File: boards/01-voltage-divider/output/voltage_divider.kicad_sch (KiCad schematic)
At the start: 4 parts, among them J1 IN, J2 OUT

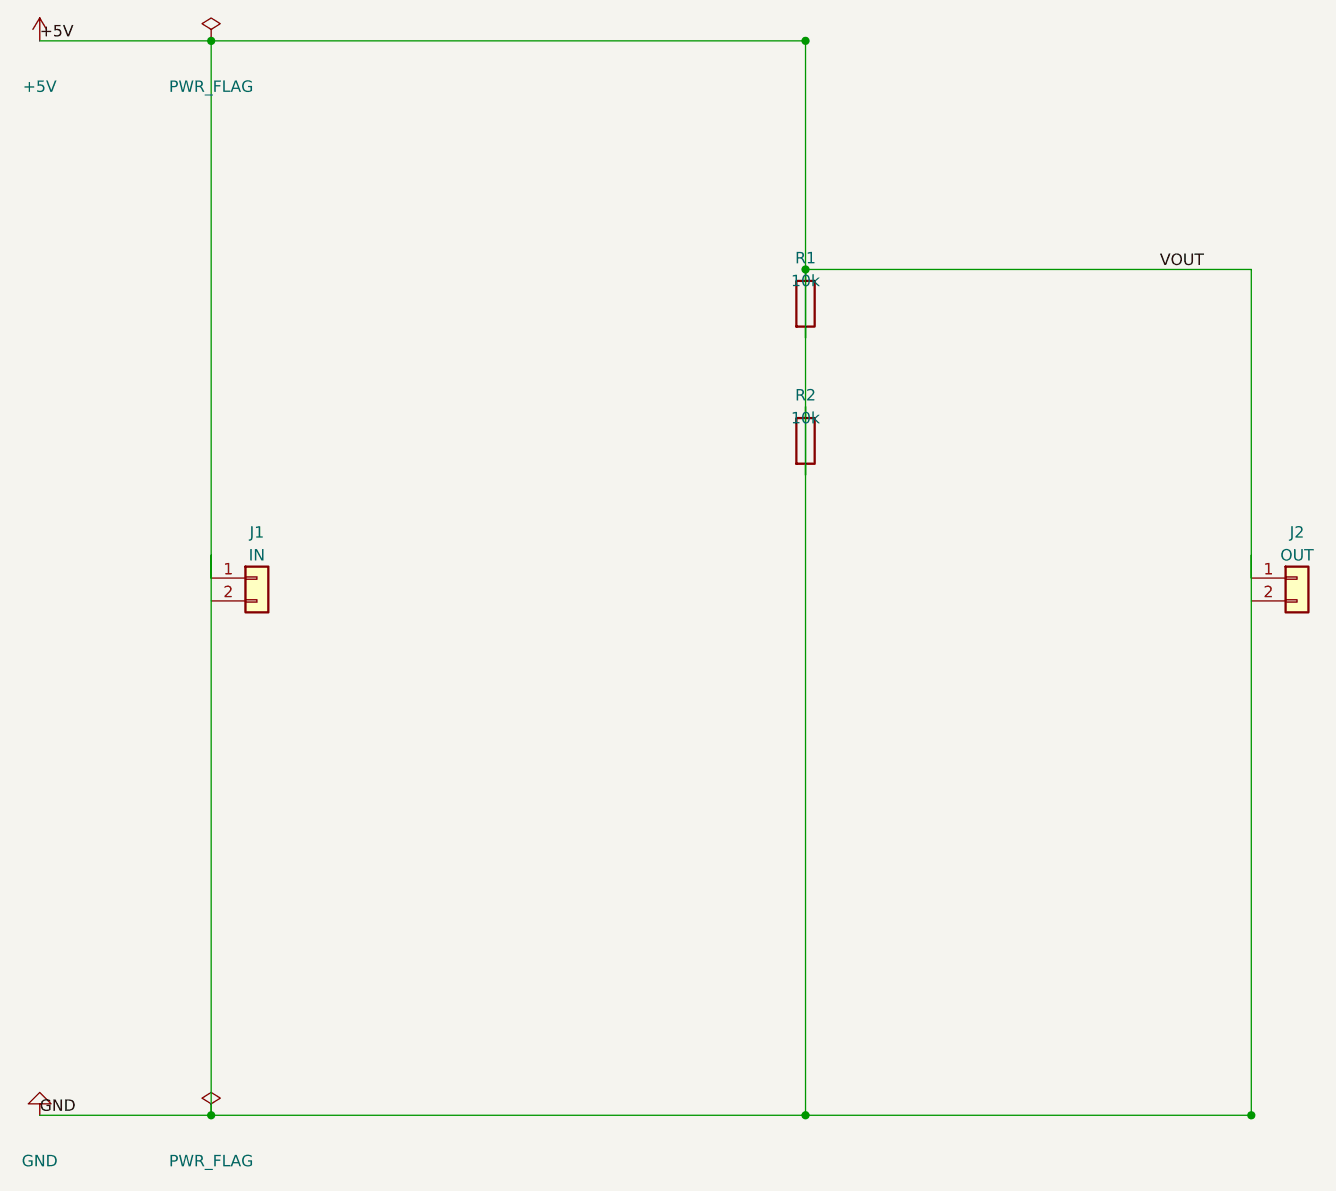
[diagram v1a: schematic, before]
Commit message: fix(board-01): migrate to negotiated router + pour-net carve-out (restore gold standard) (#3034)
* fix(board-01): migrate route step to negotiated router

Board 01's generate_design.py was calling the deprecated route_all()
entry point, which silently produced zero routed segments — VOUT in
particular had no traces on the on-disk PCB despite the script's
success counter reading 2/3 from pre-placed power-rail data.

Three coupled changes restore the gold-standard end-state:

1. Call route_all_negotiated(per_net_timeout=30.0, timeout=240.0) so
   per-net deadlines are enforced (Issue #2794 / #2775).
2. Apply the same pour-net carve-out the kct route CLI uses
   (Issue #1841): VIN and VOUT are classified as POWER by the name
   regex but this board has no copper zones, so they must route as
   signals via router._pour_nets_without_zones.
3. After routing, call cleanup_artifacts() (drops net-0 escape
   pre-pass orphans) and pass nets_to_route_ids to get_statistics()
   so the success metric matches kct route's reporting and excludes
   the intentionally-skipped GND from the denominator.

A VOUT-segment guard is added after the file write so any future
regression to the silent-zero-segments mode is loud, not silent.

Verified:
- python boards/01-voltage-divider/generate_design.py exits 0 and
  prints "Routing: SUCCESS" (was "PARTIAL: Routed 0/2 nets").
- Routed PCB has 29 (segment ...) entries (was 0); VOUT has 8.
- kct check --mfr jlcpcb: 0 errors, 4 pad_grid warnings (unchanged).
- kct fleet status: 2/3 nets complete (VIN, VOUT). GND remains
  intentionally skipped — the pre-regression gold standard never
  routed GND either (golden commit 55ac7a92: 3 VIN segs + 6 VOUT
  segs, 0 GND).

* feat(board-01): add manufacturing bundle (mfr=jlcpcb)

Generated via:
  kct export boards/01-voltage-divider/output/voltage_divider_routed.kicad_pcb --mfr jlcpcb

Brings board 01 to ship-ready parity with the other audit-tracked boards
(04/06/07) that already have manufacturing/ commi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
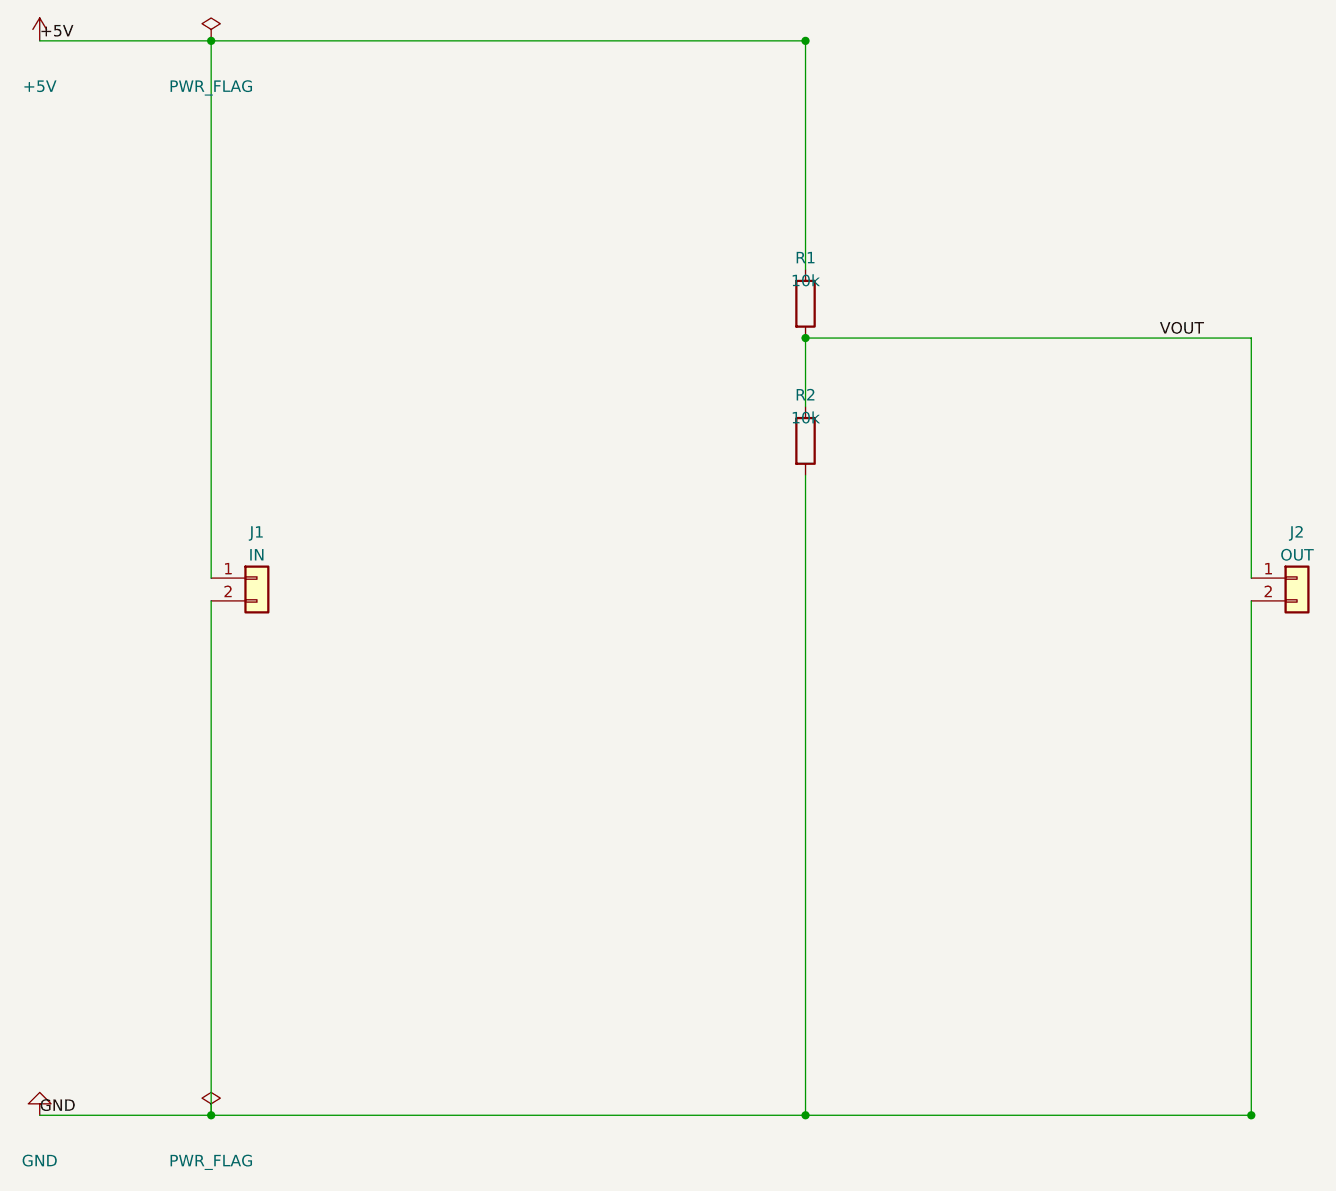
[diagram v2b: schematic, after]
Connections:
- net +5V: no longer J2.1 (Pin_1), R1.2, R2.1, R2.2
- net GND: now reaches J1.2 (Pin_2)
- net GND: now also J2.2 (Pin_2), R2.2
- new net VOUT: J2.1 (Pin_1), R1.2, R2.1
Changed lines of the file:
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@@
 		(instances
 			(project "project"
-				(path "/149338e6-b8c0-4787-8002-a53f5b29e82c" (reference "J1") (unit 1)
+				(path "/eab735e0-f8d9-4950-9b5d-95808fbf7dfa" (reference "J1") (unit 1)
 				)
 			)
@@
 		(instances
 			(project "project"
-				(path "/149338e6-b8c0-4787-8002-a53f5b29e82c" (reference "R1") (unit 1)
+				(path "/eab735e0-f8d9-4950-9b5d-95808fbf7dfa" (reference "R1") (unit 1)
 				)
 			)
@@
 		(instances
 			(project "project"
-				(path "/149338e6-b8c0-4787-8002-a53f5b29e82c" (reference "R2") (unit 1)
+				(path "/eab735e0-f8d9-4950-9b5d-95808fbf7dfa" (reference "R2") (unit 1)
 				)
 			)
@@
 		(instances
 			(project "project"
-				(path "/149338e6-b8c0-4787-8002-a53f5b29e82c" (reference "J2") (unit 1)
+				(path "/eab735e0-f8d9-4950-9b5d-95808fbf7dfa" (reference "J2") (unit 1)
 				)
 			)
@@
 		(instances
 			(project "project"
-				(path "/149338e6-b8c0-4787-8002-a53f5b29e82c" (reference "#PWR01") (unit 1)
+				(path "/eab735e0-f8d9-4950-9b5d-95808fbf7dfa" (reference "#PWR01") (unit 1)
 				)
 			)
@@
 		(instances
 			(project "project"
-				(path "/149338e6-b8c0-4787-8002-a53f5b29e82c" (reference "#PWR02") (unit 1)
+				(path "/eab735e0-f8d9-4950-9b5d-95808fbf7dfa" (reference "#PWR02") (unit 1)
 				)
 			)
@@
 		(instances
 			(project "project"
-				(path "/149338e6-b8c0-4787-8002-a53f5b29e82c" (reference "#PWR03") (unit 1)
+				(path "/eab735e0-f8d9-4950-9b5d-95808fbf7dfa" (reference "#PWR03") (unit 1)
 				)
 			)
@@
 		(instances
 			(project "project"
-				(path "/149338e6-b8c0-4787-8002-a53f5b29e82c" (reference "#PWR04") (unit 1)
+				(path "/eab735e0-f8d9-4950-9b5d-95808fbf7dfa" (reference "#PWR04") (unit 1)
 				)
 			)
@@
 	)
 	(wire
-		(pts (xy 44.45 87.63) (xy 44.45 149.86))
-		(stroke
-			(width 0)
-			(type default)
-		)
-	)
-	(wire
-		(pts (xy 110.49 63.5) (xy 110.49 30.48))
-		(stroke
-			(width 0)
-			(type default)
-		)
-	)
-	(wire
-		(pts (xy 110.49 55.88) (xy 110.49 78.74))
-		(stroke
-			(width 0)
-			(type default)
-		)
-	)
-	(wire
-		(pts (xy 110.49 71.12) (xy 110.49 149.86))
-		(stroke
-			(width 0)
-			(type default)
-		)
-	)
-	(wire
-		(pts (xy 110.49 55.88) (xy 160.02 55.88))
-		(stroke
-			(width 0)
-			(type default)
-		)
-	)
-	(wire
-		(pts (xy 160.02 55.88) (xy 160.02 90.17))
-		(stroke
-			(width 0)
-			(type default)
-		)
-	)
-	(wire
-		(pts (xy 160.02 87.63) (xy 160.02 149.86))
+		(pts (xy 44.45 92.71) (xy 44.45 149.86))
+		(stroke
+			(width 0)
+			(type default)
+		)
+	)
+	(wire
+		(pts (xy 110.49 55.88) (xy 110.49 30.48))
+		(stroke
+			(width 0)
+			(type default)
+		)
+	)
+	(wire
+		(pts (xy 110.49 63.5) (xy 110.49 71.12))
+		(stroke
+			(width 0)
+			(type default)
+		)
+	)
+	(wire
+		(pts (xy 110.49 78.74) (xy 110.49 149.86))
+		(stroke
+			(width 0)
+			(type default)
+		)
+	)
+	(wire
+		(pts (xy 110.49 63.5) (xy 160.02 63.5))
+		(stroke
+			(width 0)
+			(type default)
+		)
+	)
+	(wire
+		(pts (xy 160.02 63.5) (xy 160.02 90.17))
+		(stroke
+			(width 0)
+			(type default)
+		)
+	)
+	(wire
+		(pts (xy 160.02 92.71) (xy 160.02 149.86))
 		(stroke
 			(width 0)
@@
 	)
 	(junction
-		(at 110.49 55.88)
+		(at 110.49 63.5)
 		(diameter 0)
 	)
@@
 	)
 	(label "VOUT"
-		(at 149.86 55.88 0)
+		(at 149.86 63.5 0)
 		(fields_autoplaced yes)
 		(effects
@@
 	)
 	(sheet_instances
-		(path "/149338e6-b8c0-4787-8002-a53f5b29e82c" (page 1)
-		)
-	)
+		(path "/eab735e0-f8d9-4950-9b5d-95808fbf7dfa" (page "1")
+		)
+	)
